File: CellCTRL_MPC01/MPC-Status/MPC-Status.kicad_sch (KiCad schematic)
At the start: 33 parts, among them J1 I2C, J2 Programming, U1 ATtiny202-SS

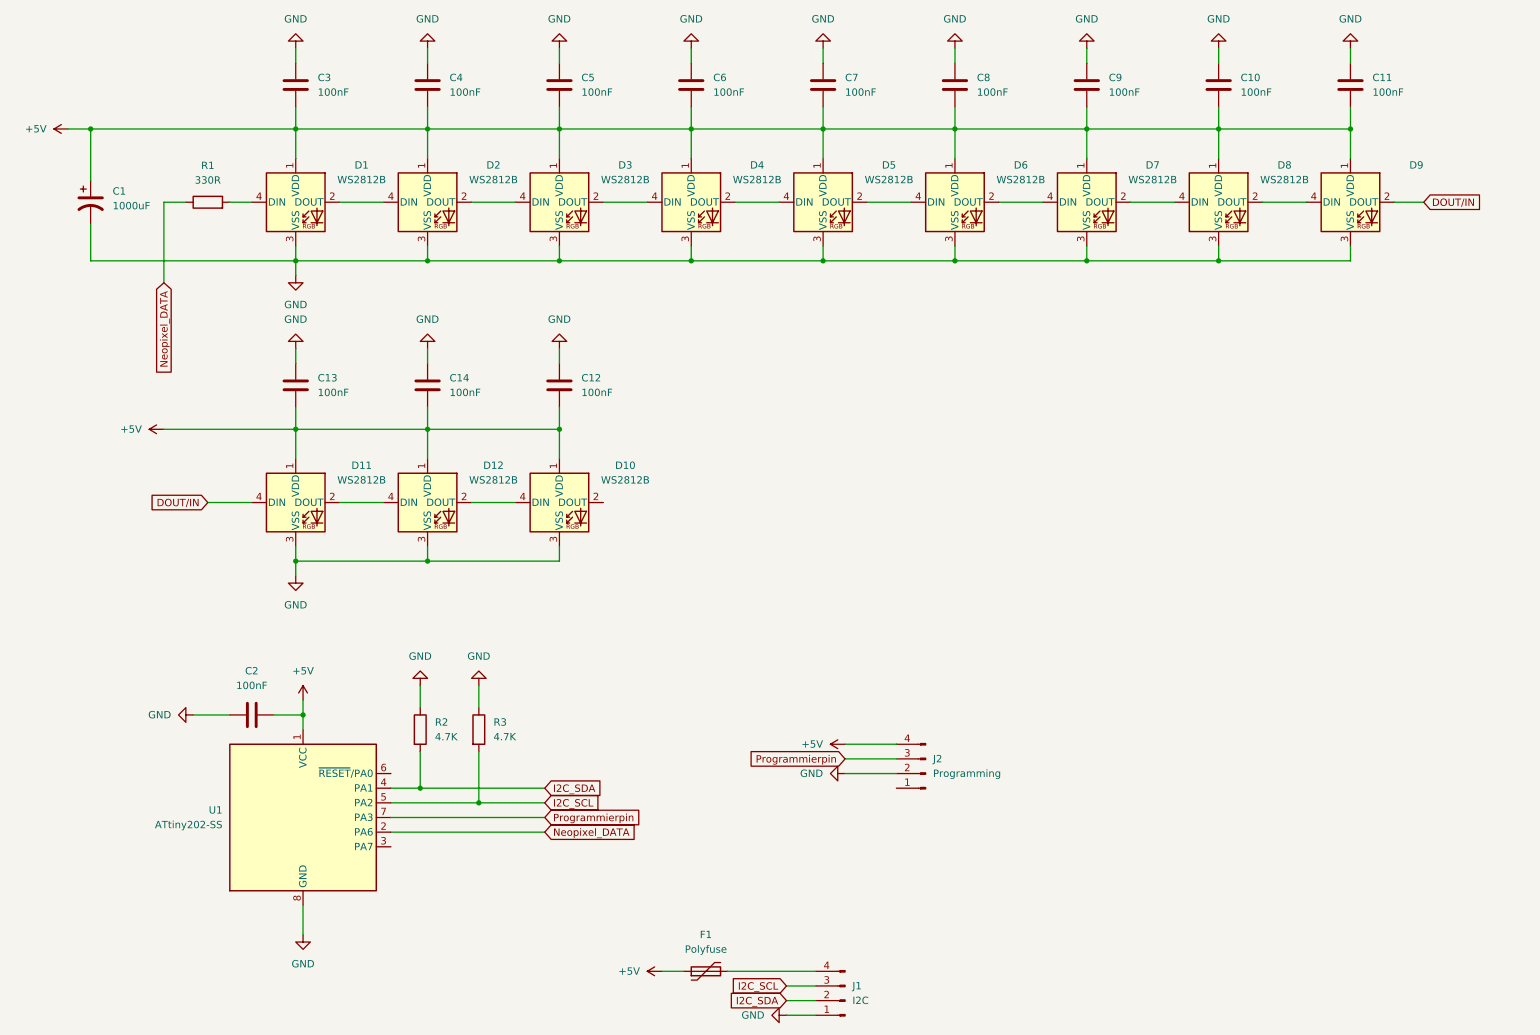
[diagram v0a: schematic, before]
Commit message: Update der PCBs
MPC01: Update der Schematics (Lötbrücken anstatt von Steckbrücken bei MSN und generell Brücken bei PDNUart)
MPC-Status: Fertigstellen des PCBs
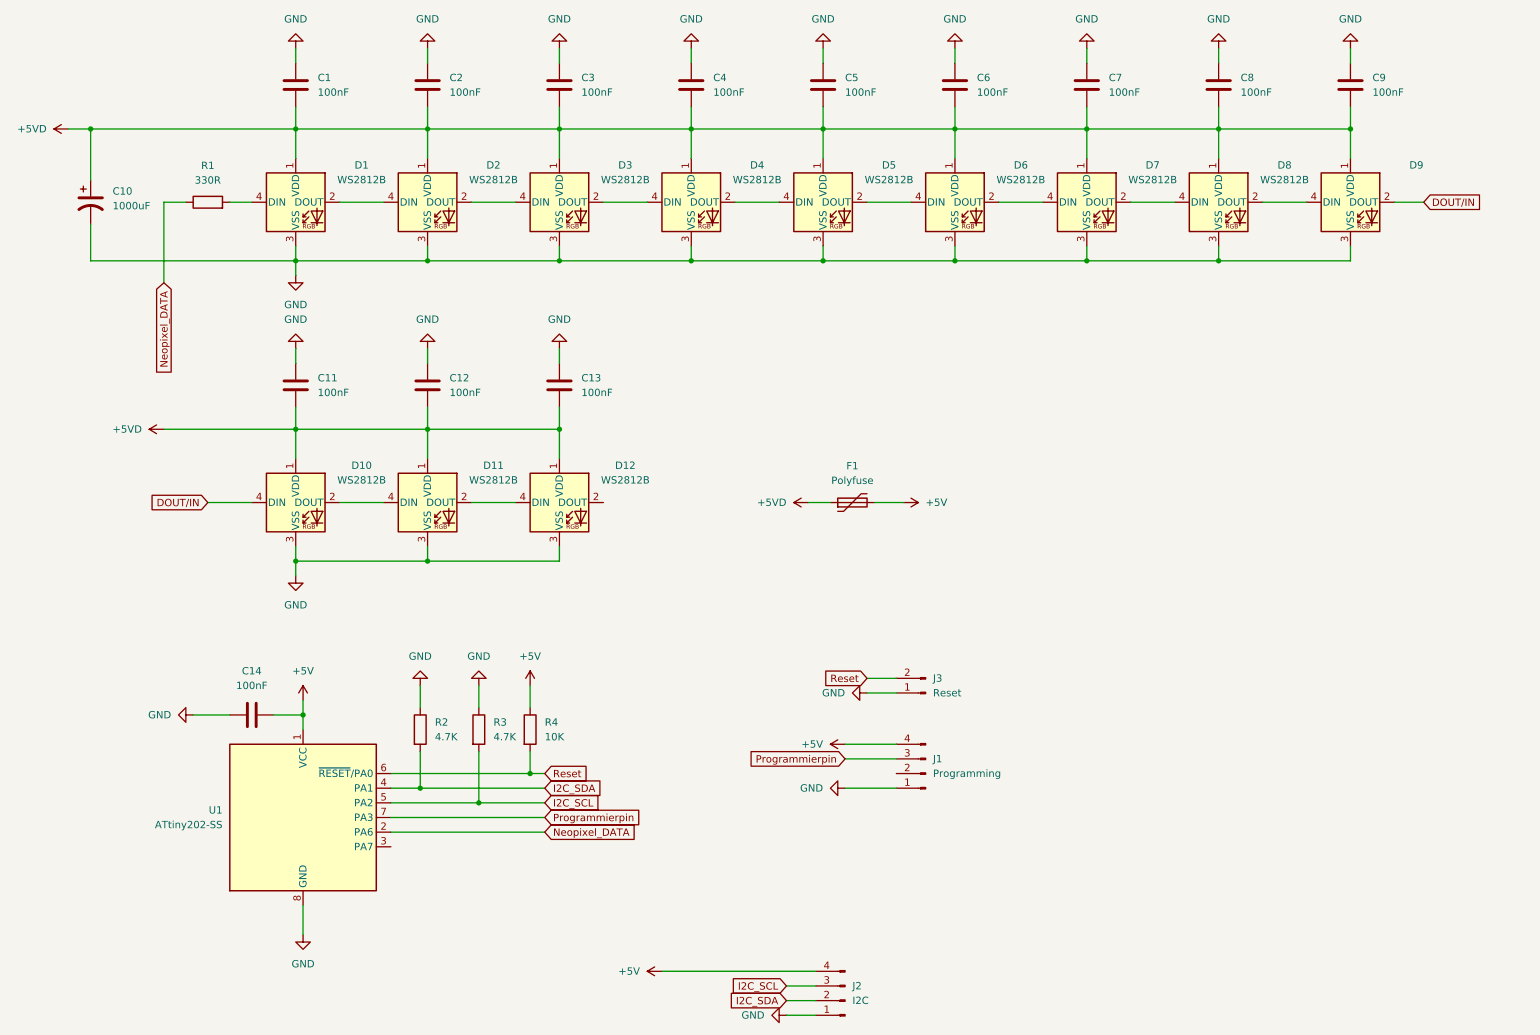
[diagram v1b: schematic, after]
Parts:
- added J3: Reset, Connector_PinHeader_2.54mm:PinHeader_1x02_P2.54mm_Vertical, symbol Connector:Conn_01x02_Pin
- added R4: 10K, Resistor_SMD:R_0805_2012Metric_Pad1.20x1.40mm_HandSolder, symbol Device:R
- J2: renamed from J1; footprint (none) -> Connector_JST:JST_EH_B4B-EH-A_1x04_P2.50mm_Vertical
- renumbered C3 to C1, C1 to C10, C13 to C11, C14 to C12, C12 to C13, C2 to C14, C4 to C2, C5 to C3, C6 to C4, C7 to C5, C8 to C6, C9 to C7, C10 to C8, C11 to C9, D11 to D10, D12 to D11, D10 to D12, J2 to J1
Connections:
- net +5V: now also F1.2, J2.4 (Pin_4), R4.1; no longer C1.1, C10.1, C11.1, C12.1, C13.1, C2.1, C3.1, C4.1, C5.1, C6.1, C7.1, C8.1, C9.1, D1.1 (VDD), D10.1 (VDD), D11.1 (VDD), D12.1 (VDD), D2.1 (VDD), D3.1 (VDD), D4.1 (VDD), D5.1 (VDD), D6.1 (VDD), D7.1 (VDD), D8.1 (VDD), D9.1 (VDD), F1.1
- net GND: now also J1.1 (Pin_1), J3.1 (Pin_1); no longer J1.2 (Pin_2)
- net Reset: now reaches U1.6 (~{RESET}/PA0)
- net Reset: now also J3.2 (Pin_2), R4.2
- new net +5VD: C1.1, C10.1, C11.1, C12.1, C13.1, C2.1, C3.1, C4.1, C5.1, C6.1, C7.1, C8.1, C9.1, D1.1 (VDD), D10.1 (VDD), D11.1 (VDD), D12.1 (VDD), D2.1 (VDD), D3.1 (VDD), D4.1 (VDD), D5.1 (VDD), D6.1 (VDD), D7.1 (VDD), D8.1 (VDD), D9.1 (VDD), F1.1
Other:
- moved on the sheet: F1

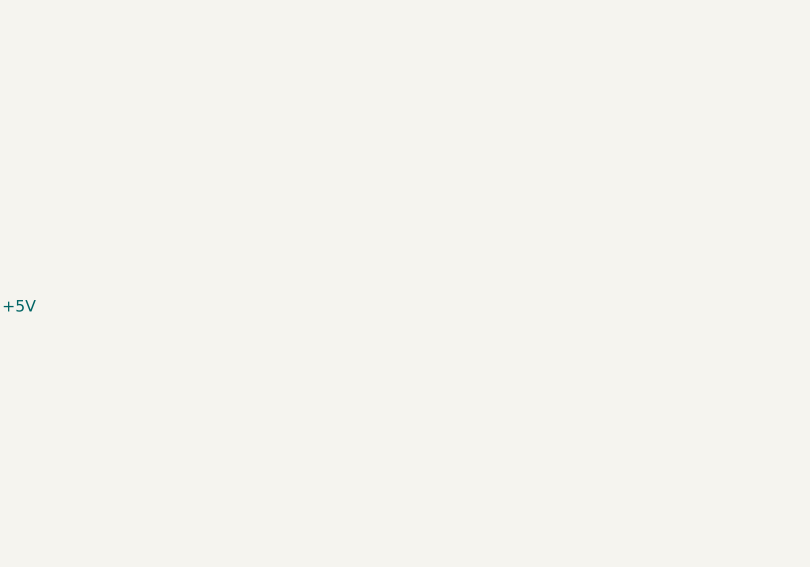
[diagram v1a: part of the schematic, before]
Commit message: Mounting Hole adds
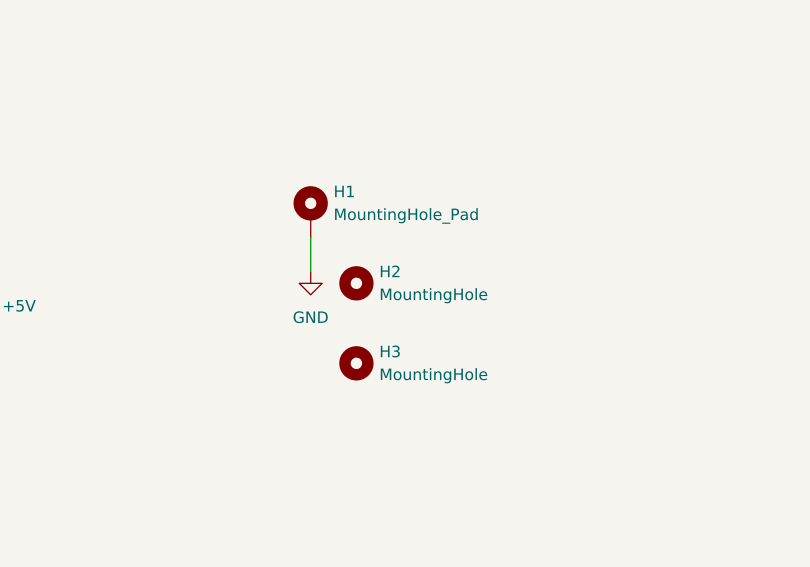
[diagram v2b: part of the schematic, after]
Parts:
- added H1: MountingHole_Pad, MountingHole:MountingHole_3.2mm_M3_DIN965_Pad, symbol Mechanical:MountingHole_Pad
- added H2, H3: MountingHole, MountingHole:MountingHole_3.2mm_M3_DIN965, symbol Mechanical:MountingHole
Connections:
- net GND: now also H1.1

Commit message: Fertig V0.1_Status
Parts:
- removed H2, H3: MountingHole, MountingHole:MountingHole_3.2mm_M3_DIN965, symbol Mechanical:MountingHole
- added H2, H3: MountingHole_Pad, MountingHole:MountingHole_3.2mm_M3_DIN965_Pad, symbol Mechanical:MountingHole_Pad
- J2: footprint Connector_JST:JST_EH_B4B-EH-A_1x04_P2.50mm_Vertical -> Connector_JST:JST_XH_B4B-XH-A_1x04_P2.50mm_Vertical
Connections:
- net GND: now also H2.1, H3.1
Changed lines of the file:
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@@
 	)
 	(junction
+		(at 227.33 93.98)
+		(diameter 0)
+		(color 0 0 0 0)
+	)
+	(junction
 		(at 82.55 148.59)
 		(diameter 0)
@@
 	)
 	(junction
+		(at 204.47 93.98)
+		(diameter 0)
+		(color 0 0 0 0)
+	)
+	(junction
 		(at 152.4 34.29)
 		(diameter 0)
@@
 	(wire
 		(pts
+			(xy 251.46 93.98) (xy 227.33 93.98)
+		)
+		(stroke
+			(width 0)
+			(type default)
+		)
+	)
+	(wire
+		(pts
 			(xy 57.15 135.89) (xy 62.23 135.89)
 		)
@@
 	(wire
 		(pts
+			(xy 251.46 91.44) (xy 251.46 93.98)
+		)
+		(stroke
+			(width 0)
+			(type default)
+		)
+	)
+	(wire
+		(pts
 			(xy 62.23 133.35) (xy 62.23 135.89)
 		)
@@
 	(wire
 		(pts
+			(xy 227.33 93.98) (xy 204.47 93.98)
+		)
+		(stroke
+			(width 0)
+			(type default)
+		)
+	)
+	(wire
+		(pts
 			(xy 160.02 46.99) (xy 167.64 46.99)
 		)
@@
 	(wire
 		(pts
-			(xy 204.47 91.44) (xy 204.47 95.25)
+			(xy 227.33 91.44) (xy 227.33 93.98)
+		)
+		(stroke
+			(width 0)
+			(type default)
+		)
+	)
+	(wire
+		(pts
+			(xy 204.47 91.44) (xy 204.47 93.98)
 		)
 		(stroke
@@
 	(wire
 		(pts
+			(xy 204.47 93.98) (xy 204.47 97.79)
+		)
+		(stroke
+			(width 0)
+			(type default)
+		)
+	)
+	(wire
+		(pts
 			(xy 198.12 39.37) (xy 198.12 34.29)
 		)
@@
 	)
 	(symbol
-		(lib_id "Mechanical:MountingHole")
-		(at 209.55 105.41 0)
-		(unit 1)
-		(exclude_from_sim no)
-		(in_bom no)
-		(on_board yes)
-		(dnp no)
-		(fields_autoplaced yes)
-		(property "Reference" "H3"
-			(at 212.09 104.1399 0)
-			(effects
-				(font
-					(size 1.27 1.27)
-				)
-				(justify left)
-			)
-		)
-		(property "Value" "MountingHole"
-			(at 212.09 106.6799 0)
-			(effects
-				(font
-					(size 1.27 1.27)
-				)
-				(justify left)
-			)
-		)
-		(property "Footprint" "MountingHole:MountingHole_3.2mm_M3_DIN965"
-			(at 209.55 105.41 0)
-			(effects
-				(font
-					(size 1.27 1.27)
-				)
-				(hide yes)
-			)
-		)
-		(property "Datasheet" "~"
-			(at 209.55 105.41 0)
-			(effects
-				(font
-					(size 1.27 1.27)
-				)
-				(hide yes)
-			)
-		)
-		(property "Description" "Mounting Hole without connection"
-			(at 209.55 105.41 0)
-			(effects
-				(font
-					(size 1.27 1.27)
-				)
-				(hide yes)
-			)
-		)
-		(instances
-			(project "MPC-Status"
-				(path "/6205391b-a61f-4e60-b73e-3eadab0d3997"
-					(reference "H3")
-					(unit 1)
-				)
-			)
-		)
-	)
-	(symbol
 		(lib_id "power:GND")
 		(at 152.4 20.32 180)
@@
 	)
 	(symbol
-		(lib_id "Mechanical:MountingHole")
-		(at 209.55 96.52 0)
-		(unit 1)
-		(exclude_from_sim no)
-		(in_bom no)
-		(on_board yes)
-		(dnp no)
-		(fields_autoplaced yes)
-		(property "Reference" "H2"
-			(at 212.09 95.2499 0)
-			(effects
-				(font
-					(size 1.27 1.27)
-				)
-				(justify left)
-			)
-		)
-		(property "Value" "MountingHole"
-			(at 212.09 97.7899 0)
-			(effects
-				(font
-					(size 1.27 1.27)
-				)
-				(justify left)
-			)
-		)
-		(property "Footprint" "MountingHole:MountingHole_3.2mm_M3_DIN965"
-			(at 209.55 96.52 0)
-			(effects
-				(font
-					(size 1.27 1.27)
-				)
-				(hide yes)
-			)
-		)
-		(property "Datasheet" "~"
-			(at 209.55 96.52 0)
-			(effects
-				(font
-					(size 1.27 1.27)
-				)
-				(hide yes)
-			)
-		)
-		(property "Description" "Mounting Hole without connection"
-			(at 209.55 96.52 0)
-			(effects
-				(font
-					(size 1.27 1.27)
-				)
-				(hide yes)
-			)
-		)
-		(instances
-			(project ""
-				(path "/6205391b-a61f-4e60-b73e-3eadab0d3997"
-					(reference "H2")
-					(unit 1)
-				)
-			)
-		)
-	)
-	(symbol
 		(lib_id "Device:C")
 		(at 175.26 26.67 180)
@@
 	(symbol
 		(lib_id "power:GND")
-		(at 204.47 95.25 0)
+		(at 204.47 97.79 0)
 		(unit 1)
 		(exclude_from_sim no)
@@
 		(fields_autoplaced yes)
 		(property "Reference" "#PWR030"
-			(at 204.47 101.6 0)
+			(at 204.47 104.14 0)
 			(effects
 				(font
@@
 		)
 		(property "Value" "GND"
-			(at 204.47 100.33 0)
+			(at 204.47 102.87 0)
 			(effects
 				(font
@@
 		)
 		(property "Footprint" ""
-			(at 204.47 95.25 0)
+			(at 204.47 97.79 0)
 			(effects
 				(font
@@
 		)
 		(property "Datasheet" ""
-			(at 204.47 95.25 0)
+			(at 204.47 97.79 0)
 			(effects
 				(font
@@
 		)
 		(property "Description" "Power symbol creates a global label with name \"GND\" , ground"
-			(at 204.47 95.25 0)
+			(at 204.47 97.79 0)
 			(effects
 				(font
@@
 	)
 	(symbol
+		(lib_id "Mechanical:MountingHole_Pad")
+		(at 251.46 88.9 0)
+		(unit 1)
+		(exclude_from_sim no)
+		(in_bom no)
+		(on_board yes)
+		(dnp no)
+		(fields_autoplaced yes)
+		(property "Reference" "H3"
+			(at 254 86.3599 0)
+			(effects
+				(font
+					(size 1.27 1.27)
+				)
+				(justify left)
+			)
+		)
+		(property "Value" "MountingHole_Pad"
+			(at 254 88.8999 0)
+			(effects
+				(font
+					(size 1.27 1.27)
+				)
+				(justify left)
+			)
+		)
+		(property "Footprint" "MountingHole:MountingHole_3.2mm_M3_DIN965_Pad"
+			(at 251.46 88.9 0)
+			(effects
+				(font
+					(size 1.27 1.27)
+				)
+				(hide yes)
+			)
+		)
+		(property "Datasheet" "~"
+			(at 251.46 88.9 0)
+			(effects
+				(font
+					(size 1.27 1.27)
+				)
+				(hide yes)
+			)
+		)
+		(property "Description" "Mounting Hole with connection"
+			(at 251.46 88.9 0)
+			(effects
+				(font
+					(size 1.27 1.27)
+				)
+				(hide yes)
+			)
+		)
+		(pin "1"
+		)
+		(instances
+			(project "MPC-Status"
+				(path "/6205391b-a61f-4e60-b73e-3eadab0d3997"
+					(reference "H3")
+					(unit 1)
+				)
+			)
+		)
+	)
+	(symbol
 		(lib_id "Device:C")
 		(at 129.54 26.67 180)
@@
 			)
 		)
-		(property "Footprint" "Connector_JST:JST_EH_B4B-EH-A_1x04_P2.50mm_Vertical"
+		(property "Footprint" "Connector_JST:JST_XH_B4B-XH-A_1x04_P2.50mm_Vertical"
 			(at 156.21 185.42 0)
 			(effects
@@
 					(unit 1)
 				)
+			)
+		)
+	)
+	(symbol
+		(lib_id "Mechanical:MountingHole_Pad")
+		(at 227.33 88.9 0)
+		(unit 1)
+		(exclude_from_sim no)
+		(in_bom no)
+		(on_board yes)
+		(dnp no)
+		(fields_autoplaced yes)
+		(property "Reference" "H2"
+			(at 229.87 86.3599 0)
+			(effects
+				(font
+					(size 1.27 1.27)
+				)
+				(justify left)
+			)
+		)
+		(property "Value" "MountingHole_Pad"
+			(at 229.87 88.8999 0)
+			(effects
+				(font
+					(size 1.27 1.27)
+				)
+				(justify left)
+			)
+		)
+		(property "Footprint" "MountingHole:MountingHole_3.2mm_M3_DIN965_Pad"
+			(at 227.33 88.9 0)
+			(effects
+				(font
+					(size 1.27 1.27)
+				)
+				(hide yes)
+			)
+		)
+		(property "Datasheet" "~"
+			(at 227.33 88.9 0)
+			(effects
+				(font
+					(size 1.27 1.27)
+				)
+				(hide yes)
+			)
+		)
+		(property "Description" "Mounting Hole with connection"
+			(at 227.33 88.9 0)
+			(effects
+				(font
+					(size 1.27 1.27)
+				)
+				(hide yes)
+			)
+		)
+		(pin "1"
+		)
+		(instances
+			(project "MPC-Status"
+				(path "/6205391b-a61f-4e60-b73e-3eadab0d3997"
+					(reference "H2")
+					(unit 1)
+				)
